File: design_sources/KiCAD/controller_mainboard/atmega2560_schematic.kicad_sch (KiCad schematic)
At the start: 15 parts, among them J4 02x03_pinheader, U1 ATmega2560-16A, Y3 16MHz

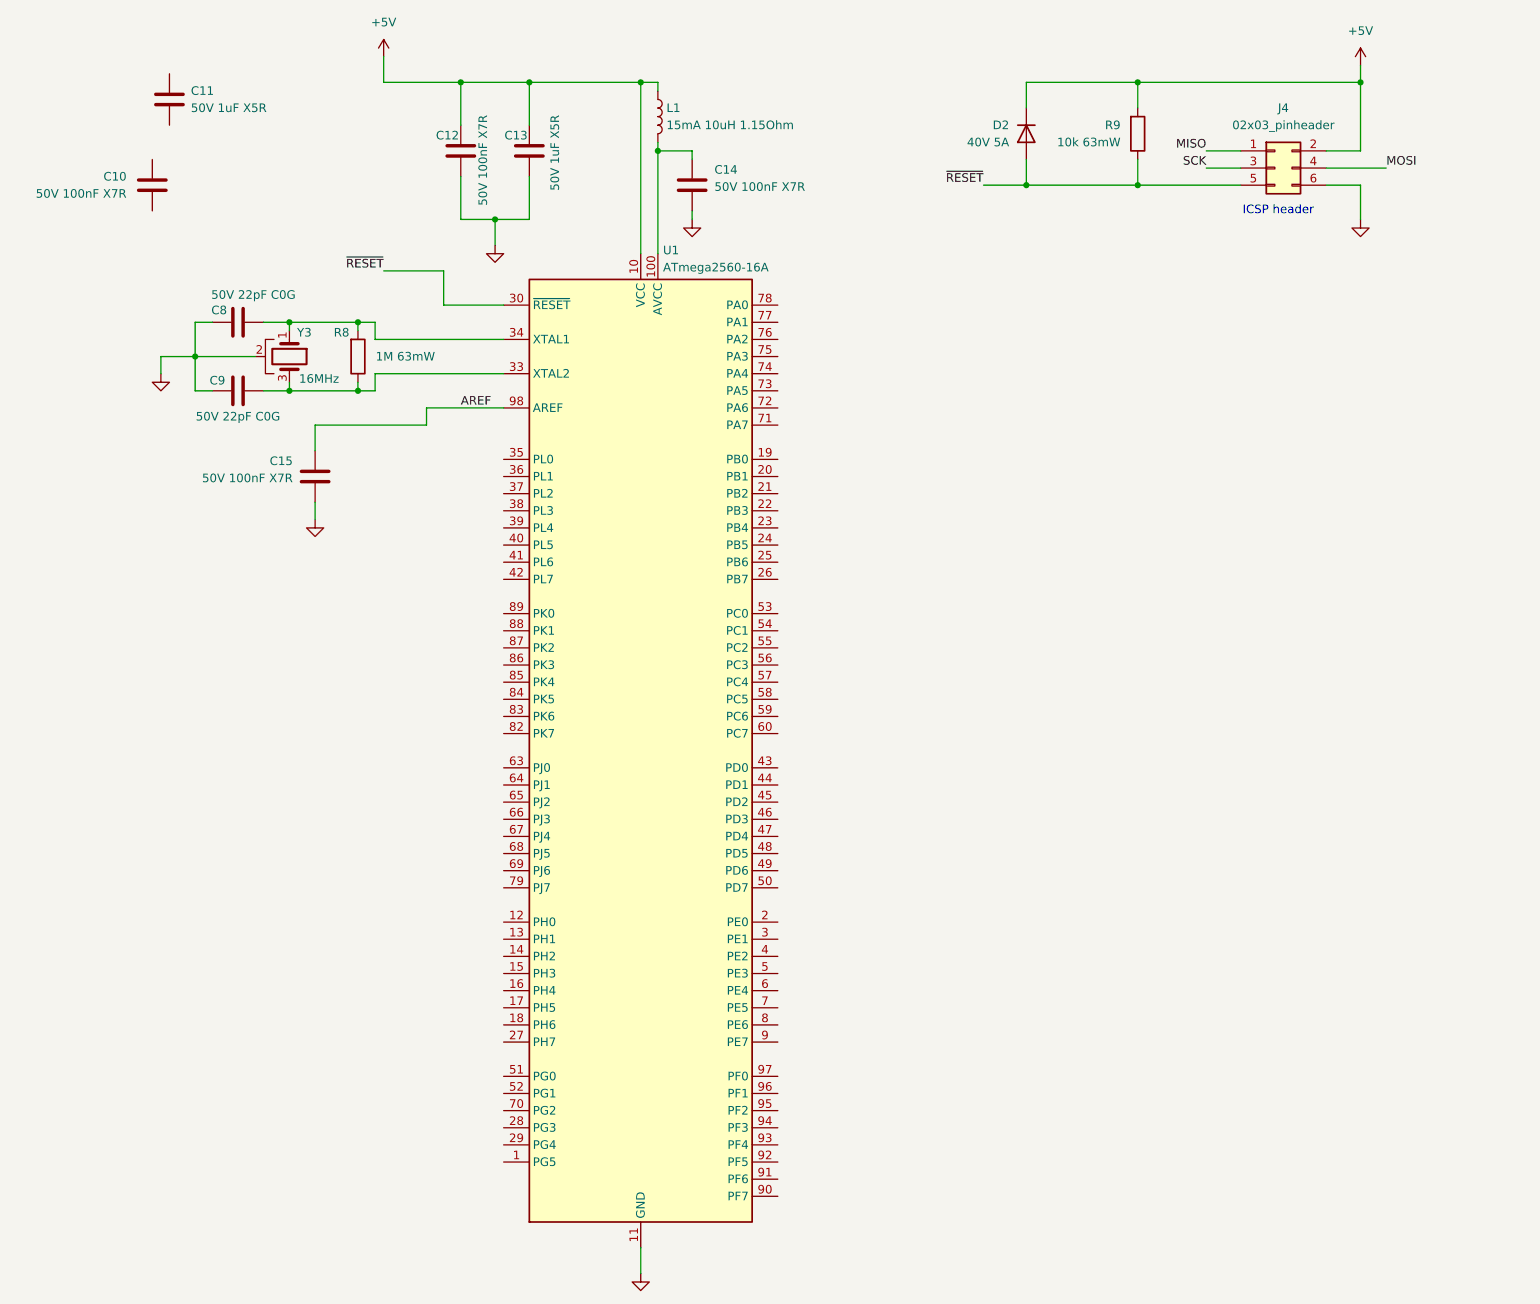
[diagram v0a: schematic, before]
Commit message: Continued development on the schematic. Pins wired. TODO validate.
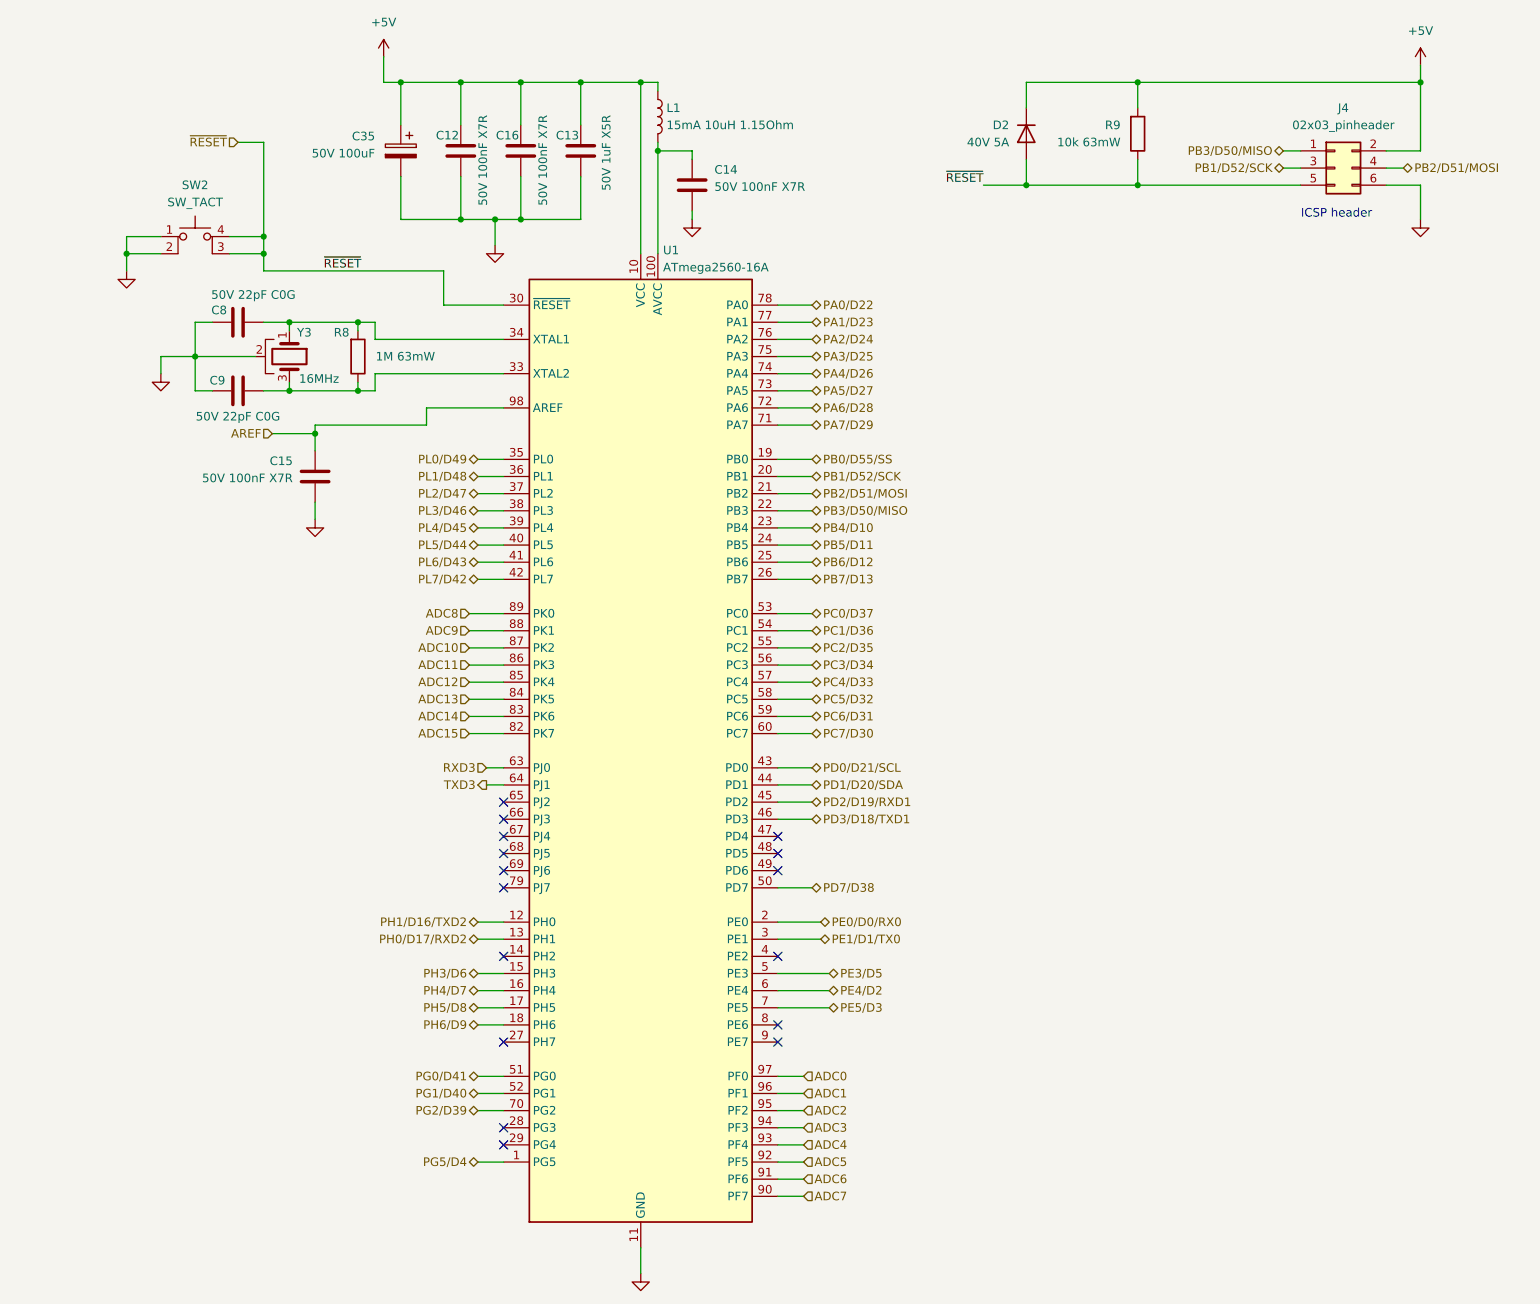
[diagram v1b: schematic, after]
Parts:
- removed C10: 50V 100nF X7R, Capacitor_SMD:C_0603_1608Metric, symbol Device:C
- removed C11: 50V 1uF X5R, Capacitor_SMD:C_0603_1608Metric, symbol Device:C
- added C16: 50V 100nF X7R, Capacitor_SMD:C_0603_1608Metric, symbol Device:C
- added C35: 50V 100uF, Capacitor_SMD:CP_Elec_8x10.5, symbol Device:C_Polarized
- added SW2: SW_TACT, Button_Switch_SMD:SW_MEC_5GSH9, symbol Switch:SW_MEC_5E
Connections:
- net MISO is gone; now on net PB3/D50/MISO: J4.1 (Pin_1)
- net MOSI is gone; now on net PB2/D51/MOSI: J4.4 (Pin_4)
- net SCK is gone; now on net PB1/D52/SCK: J4.3 (Pin_3)
- net +5V: now also C16.1, C35.1
- net GND: now also C16.2, C35.2, SW2.1, SW2.2
- net ~{RESET}: now also SW2.3 (K), SW2.4 (A)
- net PG5/D4: now reaches U1.1 (PG5)
- net PH1/D16/TXD2: now reaches U1.12 (PH0)
- net PH0/D17/RXD2: now reaches U1.13 (PH1)
- net PH3/D6: now reaches U1.15 (PH3)
- net PH4/D7: now reaches U1.16 (PH4)
- net PH5/D8: now reaches U1.17 (PH5)
- net PH6/D9: now reaches U1.18 (PH6)
- net PB0/D55/SS: now reaches U1.19 (PB0)
- net PE0/D0/RX0: now reaches U1.2 (PE0)
- net PB1/D52/SCK: now reaches U1.20 (PB1)
- net PB2/D51/MOSI: now reaches U1.21 (PB2)
- net PB3/D50/MISO: now reaches U1.22 (PB3)
- net PB4/D10: now reaches U1.23 (PB4)
- net PB5/D11: now reaches U1.24 (PB5)
- net PB6/D12: now reaches U1.25 (PB6)
- net PB7/D13: now reaches U1.26 (PB7)
- net PE1/D1/TX0: now reaches U1.3 (PE1)
- net PL0/D49: now reaches U1.35 (PL0)
- net PL1/D48: now reaches U1.36 (PL1)
- net PL2/D47: now reaches U1.37 (PL2)
- net PL3/D46: now reaches U1.38 (PL3)
- net PL4/D45: now reaches U1.39 (PL4)
- net PL5/D44: now reaches U1.40 (PL5)
- net PL6/D43: now reaches U1.41 (PL6)
- net PL7/D42: now reaches U1.42 (PL7)
- net PD0/D21/SCL: now reaches U1.43 (PD0)
- net PD1/D20/SDA: now reaches U1.44 (PD1)
- net PD2/D19/RXD1: now reaches U1.45 (PD2)
- net PD3/D18/TXD1: now reaches U1.46 (PD3)
- net PE3/D5: now reaches U1.5 (PE3)
- net PD7/D38: now reaches U1.50 (PD7)
- net PG0/D41: now reaches U1.51 (PG0)
- net PG1/D40: now reaches U1.52 (PG1)
- net PC0/D37: now reaches U1.53 (PC0)
- net PC1/D36: now reaches U1.54 (PC1)
- net PC2/D35: now reaches U1.55 (PC2)
- net PC3/D34: now reaches U1.56 (PC3)
- net PC4/D33: now reaches U1.57 (PC4)
- net PC5/D32: now reaches U1.58 (PC5)
- net PC6/D31: now reaches U1.59 (PC6)
- net PE4/D2: now reaches U1.6 (PE4)
- net PC7/D30: now reaches U1.60 (PC7)
- net RXD3: now reaches U1.63 (PJ0)
- net TXD3: now reaches U1.64 (PJ1)
- net PE5/D3: now reaches U1.7 (PE5)
- net PG2/D39: now reaches U1.70 (PG2)
- net PA7/D29: now reaches U1.71 (PA7)
- net PA6/D28: now reaches U1.72 (PA6)
- net PA5/D27: now reaches U1.73 (PA5)
- net PA4/D26: now reaches U1.74 (PA4)
- net PA3/D25: now reaches U1.75 (PA3)
- net PA2/D24: now reaches U1.76 (PA2)
- net PA1/D23: now reaches U1.77 (PA1)
- net PA0/D22: now reaches U1.78 (PA0)
- net ADC15: now reaches U1.82 (PK7)
- net ADC14: now reaches U1.83 (PK6)
- net ADC13: now reaches U1.84 (PK5)
- net ADC12: now reaches U1.85 (PK4)
- net ADC11: now reaches U1.86 (PK3)
- net ADC10: now reaches U1.87 (PK2)
- net ADC9: now reaches U1.88 (PK1)
- net ADC8: now reaches U1.89 (PK0)
- net ADC7: now reaches U1.90 (PF7)
- net ADC6: now reaches U1.91 (PF6)
- net ADC5: now reaches U1.92 (PF5)
- net ADC4: now reaches U1.93 (PF4)
- net ADC3: now reaches U1.94 (PF3)
- net ADC2: now reaches U1.95 (PF2)
- net ADC1: now reaches U1.96 (PF1)
- net ADC0: now reaches U1.97 (PF0)
- no-connect marks 0 -> 16
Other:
- company: Kestech -> Mete Han Keskin
- moved on the sheet: C13, J4
